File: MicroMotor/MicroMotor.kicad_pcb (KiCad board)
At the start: 4 copper layers, 76.9 x 37 mm, 84 parts, among them J1 USB_B_Micro, J2 Conn_01x04_Male, J3 Conn_01x05_Male, J4 Conn_01x02_Female, J5 Conn_01x11_Female, Q1 CSD18537NQ5A, Q2 CSD18537NQ5A, Q3 CSD18537NQ5A, Q4 CSD18537NQ5A, Q5 CSD18537NQ5A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

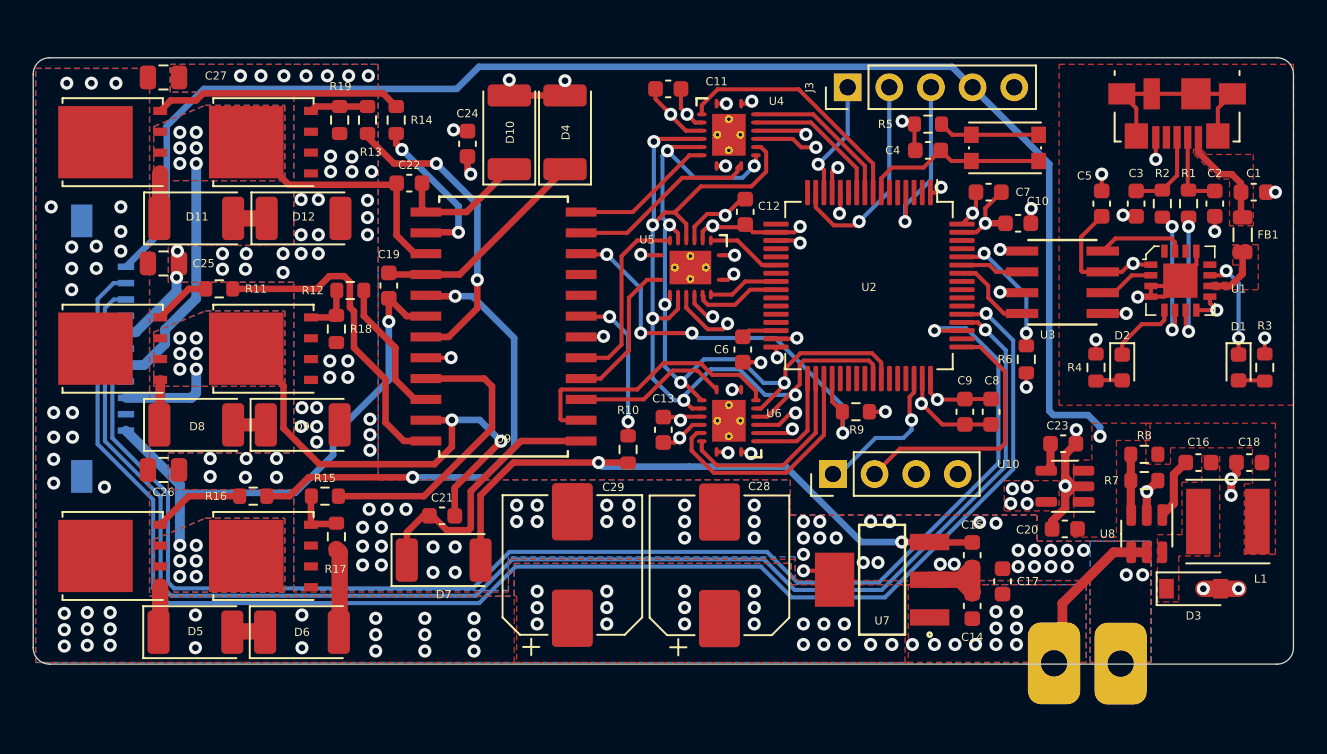
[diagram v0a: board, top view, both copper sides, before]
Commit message: Totally changed MOSFET layout. Added PWR and enabled LEDs
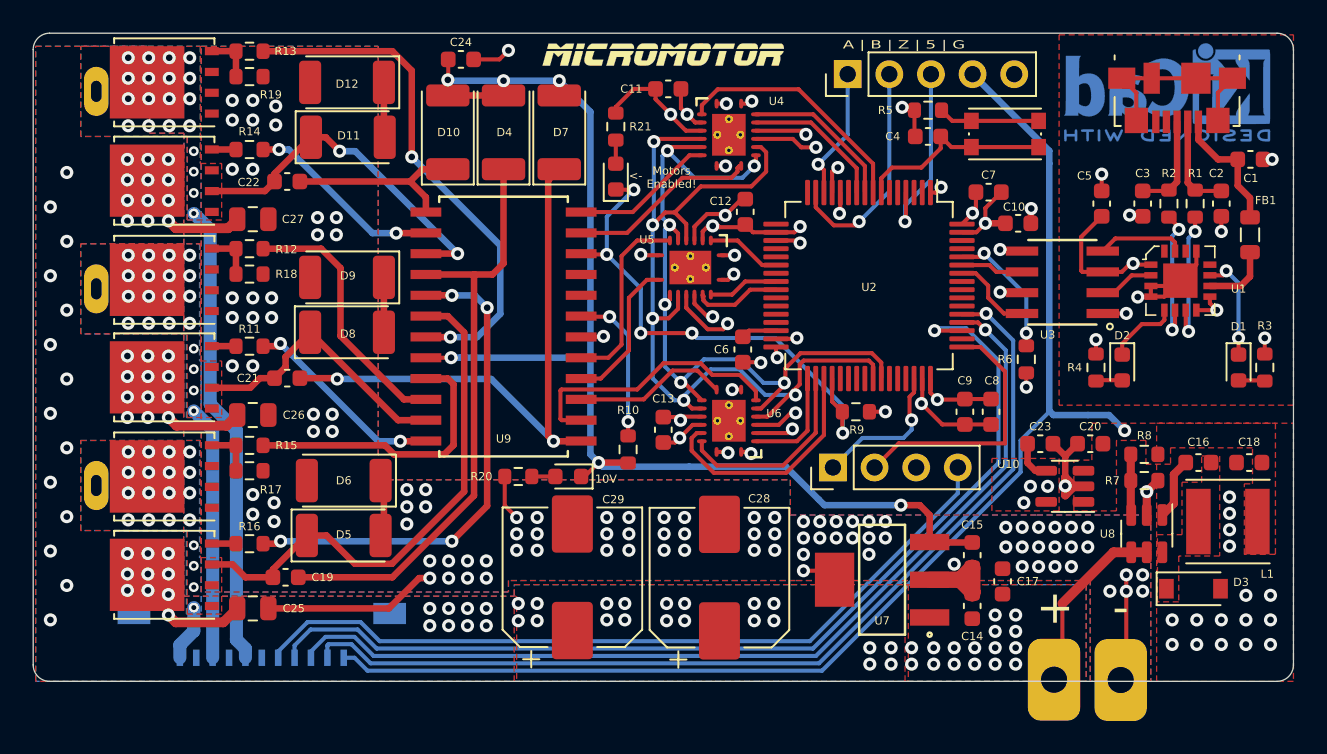
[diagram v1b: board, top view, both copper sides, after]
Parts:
- added D13: LED, LED_SMD:LED_0603_1608Metric, F.Cu at (140.2, 97.2)
- added D14: LED, LED_SMD:LED_0603_1608Metric, F.Cu at (143.1, 79.0)
- added G***: LOGO, kyleRhess_logos:logo_blackmesa, B.Cu at (124.3, 98.0)
- added G***: LOGO, kyleRhess_logos:muMotor_logo, F.Cu at (146.0, 71.5)
- added R20: 10k, Resistor_SMD:R_0603_1608Metric, F.Cu at (137.1, 97.2)
- added R21: 330, Resistor_SMD:R_0603_1608Metric, F.Cu at (143.1, 75.9)
- added REF**: KiCad-Logo2_5mm_Copper, Symbol:KiCad-Logo2_5mm_Copper, B.Cu at (176.7, 73.8)
- added REF**: TestPoint_THTPad_D1.0mm_Drill0.5mm, TestPoint:TestPoint_THTPad_D1.0mm_Drill0.5mm, F.Cu at (111.3, 96.8)
- added REF**: TestPoint_THTPad_D1.0mm_Drill0.5mm, TestPoint:TestPoint_THTPad_D1.0mm_Drill0.5mm, F.Cu at (111.3, 84.8)
- added REF**: TestPoint_THTPad_D1.0mm_Drill0.5mm, TestPoint:TestPoint_THTPad_D1.0mm_Drill0.5mm, F.Cu at (111.3, 72.8)
- added REF**: WEEE-Logo_4.2x6mm_SilkScreen, Symbol:WEEE-Logo_4.2x6mm_SilkScreen, B.Cu at (158.7, 86.0)
- moved D7 27.0 mm to (139.6, 76.2), turned to 90 degrees
- moved C25 21.7 mm to (120.9, 105.3)
- moved J5 20.2 mm to (121.5, 107.4), turned to 0 degrees
- moved C19 18.9 mm to (122.9, 103.4), turned to 180 degrees
- moved C21 12.6 mm to (123.0, 91.2), turned to 180 degrees
- moved D5 10.8 mm to (126.5, 100.8)
- moved D8 10.8 mm to (126.7, 88.5)
- moved D11 10.5 mm to (126.7, 76.5)
- moved C27 10.2 mm to (120.9, 81.5)
- moved D6 9.60 mm to (126.5, 97.5), turned to 180 degrees
- moved D9 9.40 mm to (126.7, 85.1), turned to 180 degrees
- moved R14 9.13 mm to (120.7, 77.3), turned to 180 degrees
- moved D12 8.71 mm to (126.7, 73.2), turned to 180 degrees
- moved R13 8.34 mm to (120.7, 71.3), turned to 180 degrees
- moved Q2 7.75 mm to (115.5, 97.2)
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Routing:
- net GND: track 79.8 -> 133.4 mm, vias 128 -> 143
- net +10V: track 46.6 -> 77.6 mm
- net HALL_C: track 90.7 -> 59.7 mm
- net HALL_A: track 86.9 -> 58.9 mm
- net HALL_B: track 86.7 -> 62.0 mm
- net AHB: track 13.5 -> 37.1 mm
- net BHB: track 16.7 -> 35.8 mm, vias 0 -> 2
- net +VDC: track 8.09 -> 25.2 mm, vias 71 -> 92
- net MTR_C: track 33.2 -> 49.9 mm, vias 6 -> 22
- net CHO: track 15.2 -> 1.48 mm
- net Net-(R13-Pad1): track 18.8 -> 31.8 mm
- net 5V_Out: track 86.6 -> 78.7 mm
- net Net-(R12-Pad1): track 8.61 -> 16.2 mm
- net Net-(R11-Pad1): track 20.0 -> 12.5 mm, vias 0 -> 2
- net MTR_B: track 38.5 -> 32.6 mm, vias 8 -> 20
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- removed copper zone on In2.Cu, net +10V
- removed copper zone on F.Cu, net Net-(C1-Pad1)
- removed copper zone on F.Cu, net Net-(FB1-Pad1)
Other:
- board size 76.9 x 37 mm -> 76.9 x 39.5 mm
- board text added: "+"
- board text added: "-"
- board text added: "10V"
- board text added: "<-"
- board text added: "A | B | Z | 5 | G"
- board text added: "Motors Enabled!"
- board text added: "RX"
- board text added: "TX"

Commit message: Exposed hall nets for external use
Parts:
- removed the REF** at (111.3, 96.8)
- removed the REF** at (111.3, 84.8)
- added G***: LOGO, kyleRhess_logos:logo_foxhound, B.Cu at (179.2, 94.5)
- added J8: Conn_01x01_Male, Connector_Pin:Pin_D0.5mm_L6.5mm_W1.8mm_FlatFork, F.Cu at (113.2, 108.3)
- added J8: Conn_01x01_Male, Connector_Pin:Pin_D0.5mm_L6.5mm_W1.8mm_FlatFork, F.Cu at (112.1, 108.3)
- added J8: Conn_01x01_Male, Connector_Pin:Pin_D0.5mm_L6.5mm_W1.8mm_FlatFork, F.Cu at (111.0, 108.3)
- added J8: Conn_01x01_Male, Connector_Pin:Pin_D0.5mm_L6.5mm_W1.8mm_FlatFork, F.Cu at (109.9, 108.3)
- added REF**: TestPoint_THTPad_D1.0mm_Drill0.5mm, TestPoint:TestPoint_THTPad_D1.0mm_Drill0.5mm, F.Cu at (111.2, 96.8)
- added REF**: TestPoint_THTPad_D1.0mm_Drill0.5mm, TestPoint:TestPoint_THTPad_D1.0mm_Drill0.5mm, F.Cu at (111.2, 84.8)
- moved C17 0.25 mm to (166.4, 103.7)
- moved REF** 0.15 mm to (111.2, 72.8)
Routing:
- net HALL_C: track 59.7 -> 76.7 mm, vias 1 -> 2
- net HALL_A: track 58.9 -> 73.6 mm, vias 1 -> 2
- net HALL_B: track 62.0 -> 74.7 mm, vias 1 -> 2
- net GND: track 133.4 -> 142.8 mm, vias 143 -> 150
- net MTR_A: vias 20 -> 19
- net +VDC: vias 92 -> 124
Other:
- board text added: "A"
- board text added: "B"
- board text added: "C"
- board text added: "GND"
- board text added: "HA"
- board text added: "HB"
- board text added: "HC"
- board text added: "Power"
- board text removed: "10V"

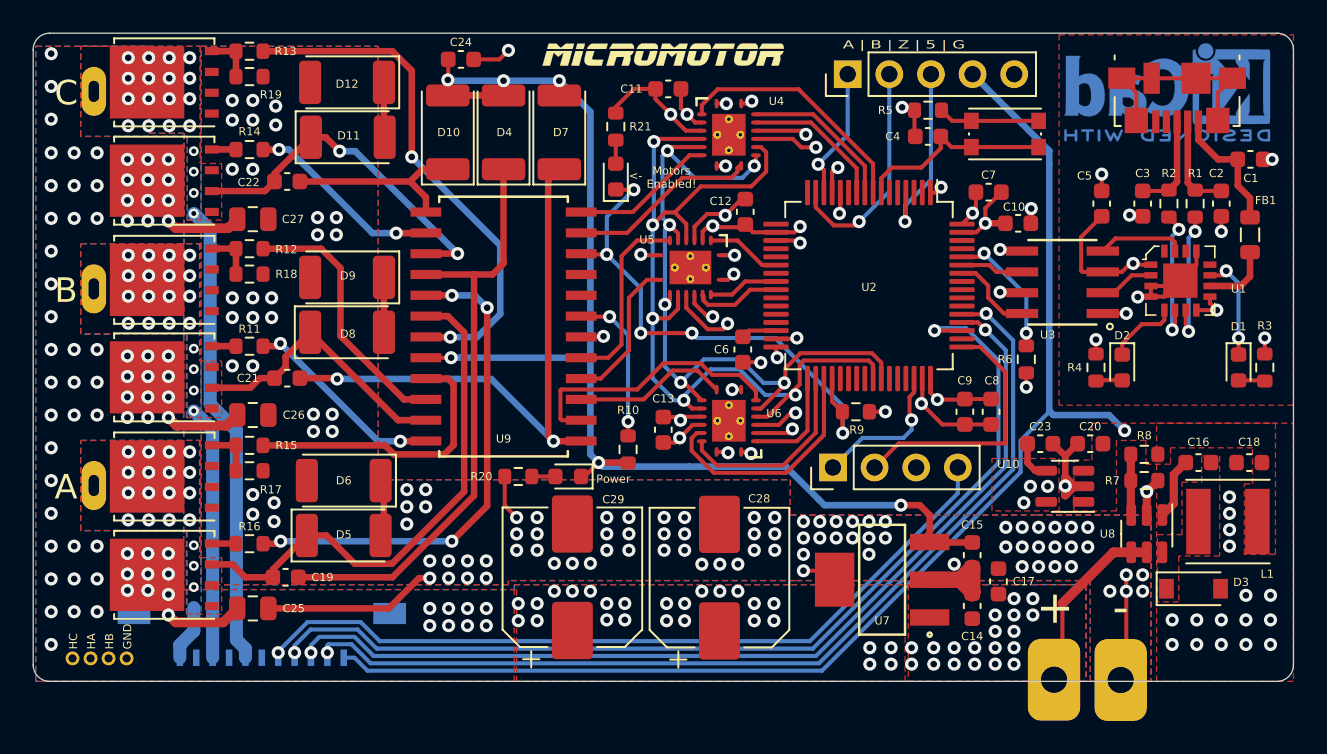
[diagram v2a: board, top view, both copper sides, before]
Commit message: Added inverter logic to USB side since isolator inverts signals. Added pull-ups on optoisolator. Fix some silkscreens.
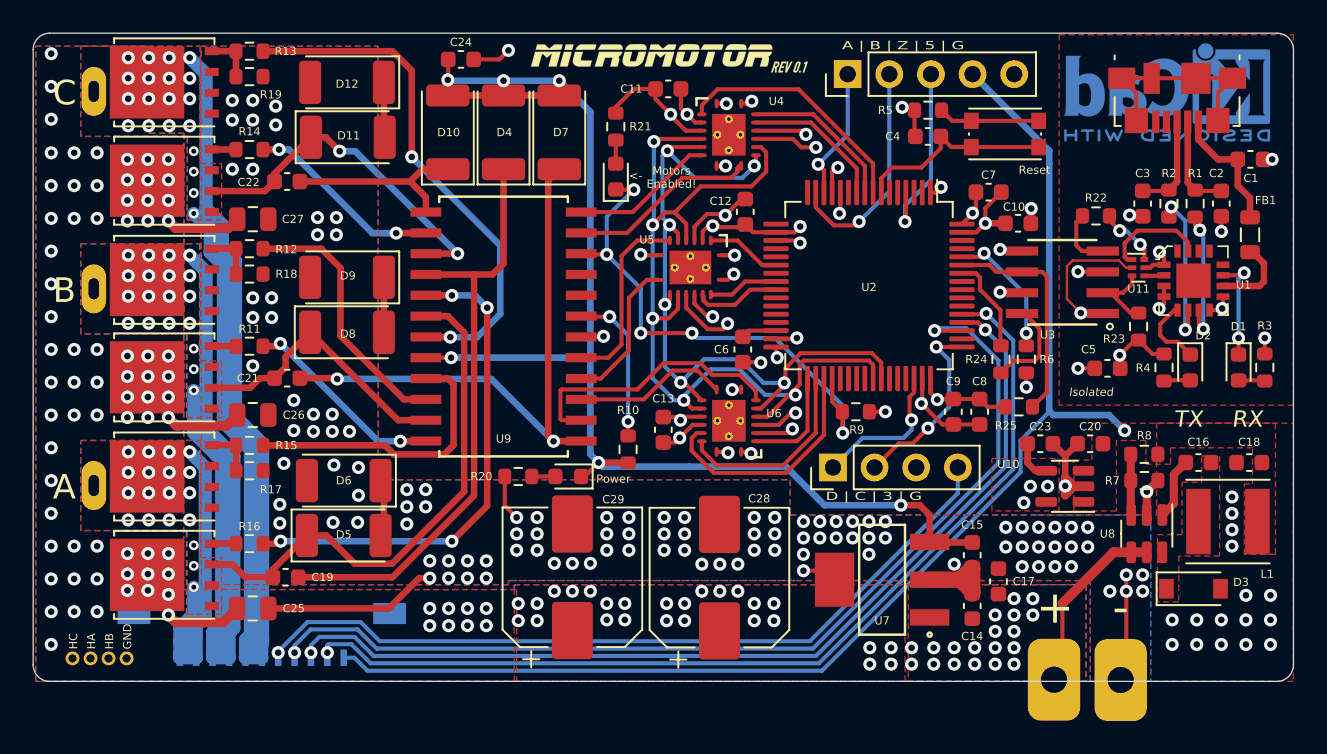
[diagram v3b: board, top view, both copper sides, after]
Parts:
- added G***: LOGO, kyleRhess_logos:kylerhess_github, B.Cu at (145.8, 108.1)
- added G***: LOGO, kyleRhess_logos:rev_0p1, F.Cu at (153.7, 72.2)
- added R22: 330, Resistor_SMD:R_0603_1608Metric, F.Cu at (172.3, 81.3)
- added R23: 1k, Resistor_SMD:R_0603_1608Metric, F.Cu at (174.9, 88.1)
- added R24: 330, Resistor_SMD:R_0603_1608Metric, F.Cu at (166.6, 90.1)
- added R25: 1k, Resistor_SMD:R_0603_1608Metric, F.Cu at (167.7, 93.0)
- added U11: NC7WZ04, Package_SON:Fairchild_MicroPak-6_1.0x1.45mm_P0.5mm, F.Cu at (174.9, 84.5)
- R17, R18, R19, R9: value 50k -> 100k
- U1: value FT230XQ-R -> FT230XQ-T
- moved G*** 49.7 mm to (173.9, 101.2)
- moved C5 10.1 mm to (173.1, 90.7), turned to 180 degrees
- moved D2 4.15 mm to (178.1, 90.6)
- moved R4 4.15 mm to (176.5, 90.6)
- moved U1 0.80 mm to (178.3, 85.3)
- moved G*** 0.70 mm to (145.3, 71.5)
- moved C8 0.70 mm to (165.2, 93.3)
- moved C9 0.70 mm to (163.7, 93.3)
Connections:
- J5 pad 2: Net-(J5-Pad2) -> MTR_A
- J5 pad 4: Net-(J5-Pad4) -> MTR_B
- J5 pad 6: Net-(J5-Pad6) -> MTR_C
- U1 pad 2: RXD -> -RXD
- U3 pad 4: Net-(U1-Pad15) -> Net-(R22-Pad1)
- U3 pad 8: USART1_TX -> Net-(R24-Pad1)
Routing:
- net MTR_C: track 49.9 -> 91.2 mm
- net MTR_B: track 32.6 -> 63.4 mm, vias 20 -> 19
- net MTR_A: track 35.5 -> 55.4 mm
- net USART1_RX: track 3.83 -> 13.8 mm
- net Net-(R24-Pad1): track 0.00 -> 5.89 mm
- net SWCLK: track 16.2 -> 11.6 mm, vias 0 -> 2
- net Net-(R22-Pad2): track 0.00 -> 3.78 mm, vias 0 -> 2
- net Net-(R22-Pad1): track 0.00 -> 3.71 mm
- net +10V: track 77.6 -> 81.0 mm
- net RXD: track 3.38 -> 5.19 mm
- net 3v3Out: track 12.5 -> 10.7 mm, vias 4 -> 5
- net Net-(R2-Pad1): track 8.57 -> 9.81 mm
- net -RXD: track 0.00 -> 1.21 mm
- net +3V3: track 42.8 -> 43.9 mm
- net GNDS: track 12.6 -> 13.7 mm
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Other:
- rule trace_min: 0.2 -> 0.13
- rule via_min_size: 0.4 -> 0.3
- board text added: "D | C | 3 | G"
- board text added: "Isolated"
- board text added: "Reset"

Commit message: Ordered boards
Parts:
- added G***: LOGO, kyleRhess_logos:11082020, B.Cu at (131.9, 71.8)
- added G***: LOGO, kyleRhess_logos:403a183, B.Cu at (146.6, 71.8)
